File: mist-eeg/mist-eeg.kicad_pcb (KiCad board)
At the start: 4 copper layers, 50 x 75 mm, 186 parts, among them J1 Power_6.5V-14V, J2 Audio, J3 Electrodes, J4 Molex 104031, J5 Extra GPIOs, J6 Digital buses, J7 J1312, J8 J1311, J9 J1310, Q1 NMOS_DGS (3V3), Q2 NMOS_DGS (3.3V), Q3 NMOS_DGS (3.3V), Q4 PMOS_DGS (3.3V @ 1A), SW1 START, SW2 USER, SW3 SD_RST, SW4 RESET, SW5 ONOFF, U1 LTC2947, U2 TSR_1-2433, U3 TSR_2-2450, U4 LT3042xMSE, U5 LT3042xMSE, U6 SGTL5000XNAA3, U7 ADS1299, U8 NX5427001Z

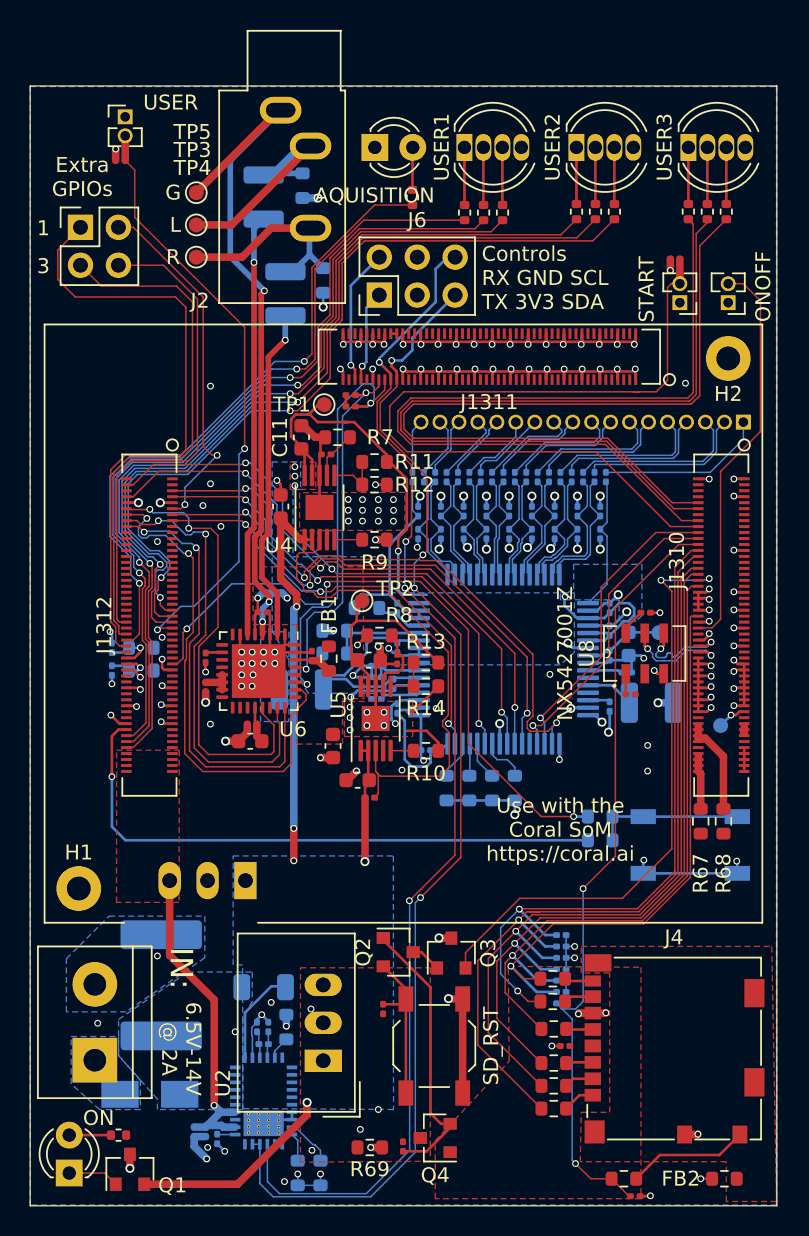
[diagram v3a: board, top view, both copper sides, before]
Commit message: Switch to bigger min via size
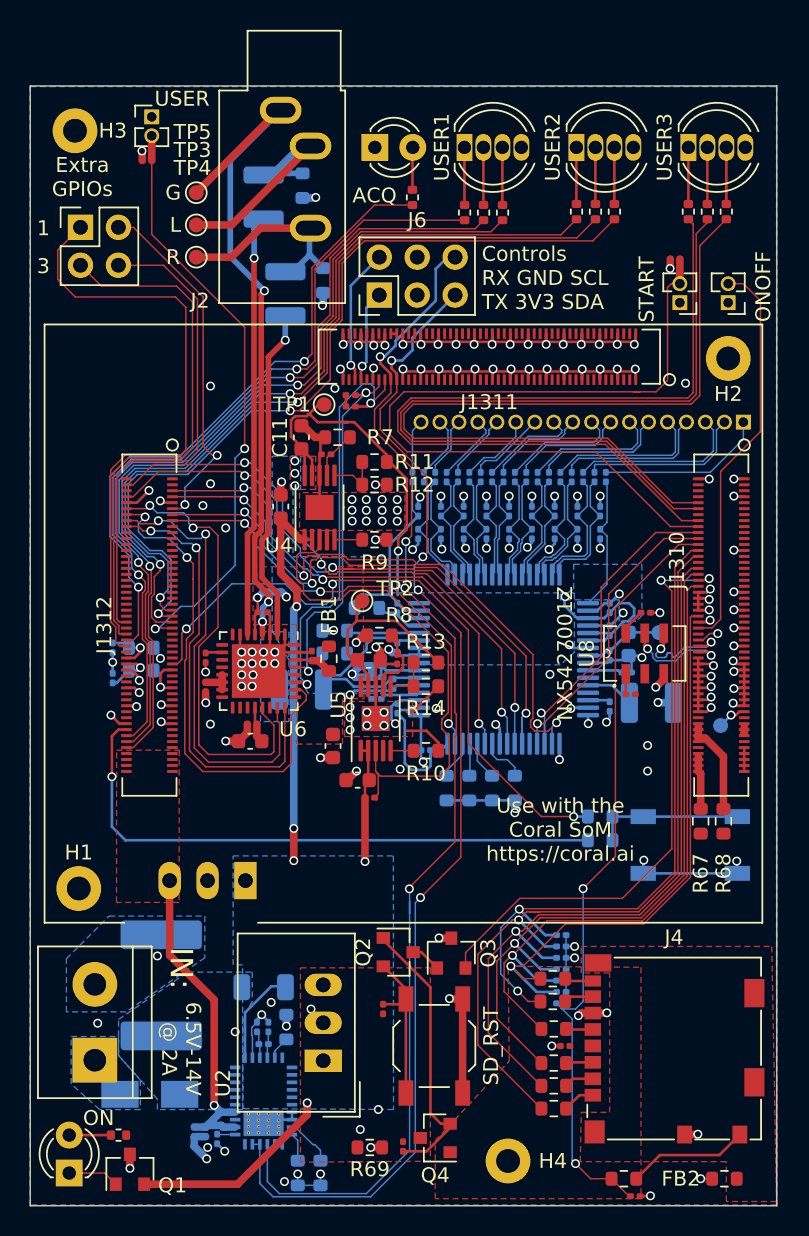
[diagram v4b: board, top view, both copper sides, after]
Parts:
- added H3: MountingHole, mist-eeg:MountingHole_1.6mm, F.Cu at (202.0, 37.0)
- added H4: MountingHole, mist-eeg:MountingHole_1.6mm, F.Cu at (231.0, 106.0)
- D3: value AQUISITION -> ACQ
- J4: value Molex 104031 -> Micro_SD_Card_Det
- moved R56 1.78 mm to (206.8, 39.0)
- moved SW2 1.78 mm to (207.1, 36.1)
- moved R73 0.51 mm to (204.5, 73.7), turned to 270 degrees
- moved R75 0.05 mm to (204.5, 71.6), turned to 90 degrees
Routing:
- net /EEG_START: track 36.5 -> 38.5 mm
- net /+5V0_ANA: track 58.0 -> 56.1 mm
- net /~EEG_PWDN~: track 20.3 -> 21.9 mm
- net GND: track 256.3 -> 257.8 mm, vias 176 -> 173
- net /CTRL_SCL: track 79.8 -> 80.9 mm
- net /~EEG_CS~: track 38.9 -> 40.0 mm
- net /USER: track 40.4 -> 39.6 mm
- net /AUDIO_SCL: track 23.9 -> 24.6 mm
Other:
- net class Audio: via_dia 0.4572 -> 0.6; via_drill 0.3048 -> 0.4
- net class Default: via_dia 0.4572 -> 0.6; via_drill 0.3048 -> 0.4
- net class Ground: via_dia 0.6096 -> 0.6; via_drill 0.381 -> 0.4
- net class Power: via_dia 0.6096 -> 0.6; via_drill 0.381 -> 0.4
- net class Shield: via_dia 0.6096 -> 0.6; via_drill 0.3048 -> 0.4
- net class USB cc removed
- rule via_min_drill: 0.299999 -> 0.4
- rule via_min_size: 0.452399 -> 0.6
